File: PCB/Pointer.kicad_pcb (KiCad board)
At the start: 2 copper layers, 81.3 x 63.5 mm, 9 parts, among them J1 Conn_01x20, J2 Conn_01x20, J3 Conn_01x05_Pin, J4 Screw_Terminal_01x02, J5 Conn_01x03_Pin, U1 ULN2003

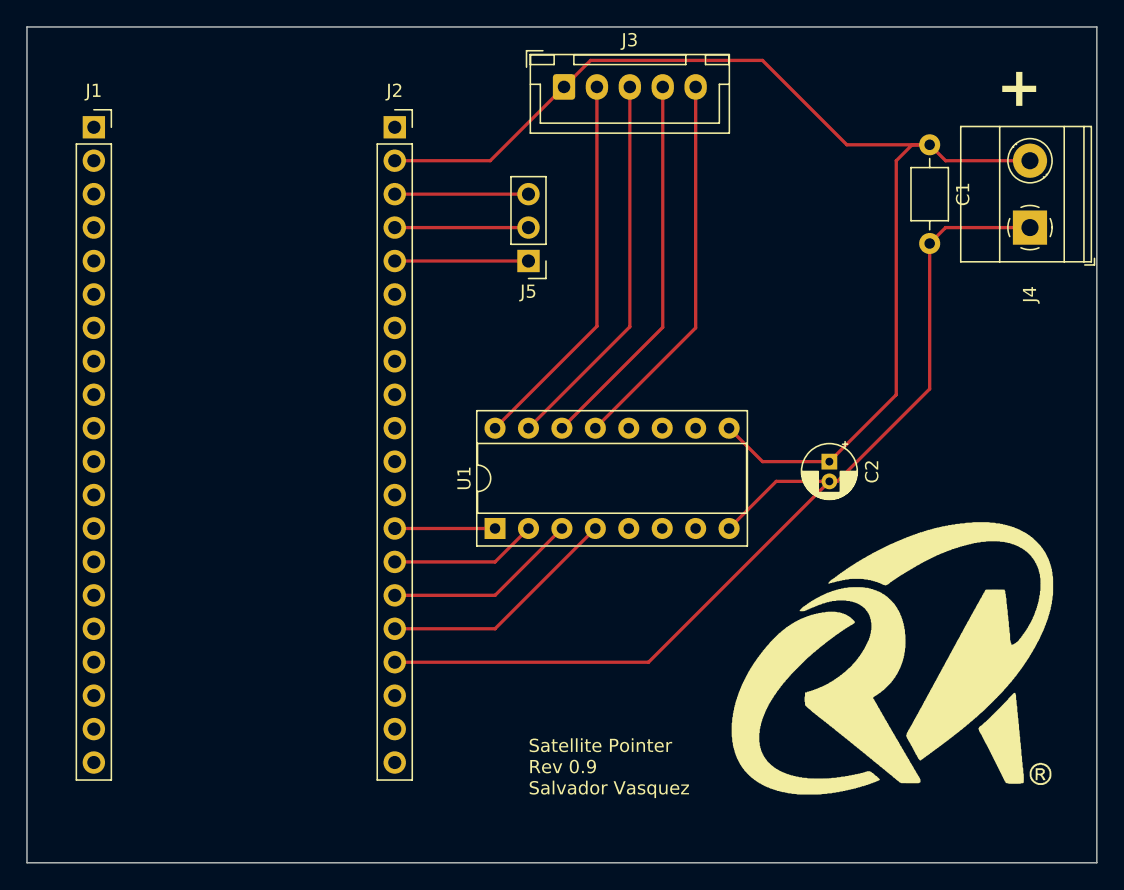
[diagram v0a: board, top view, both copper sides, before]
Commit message: PCB Rev 1.0
Fixed MCU and servo headers
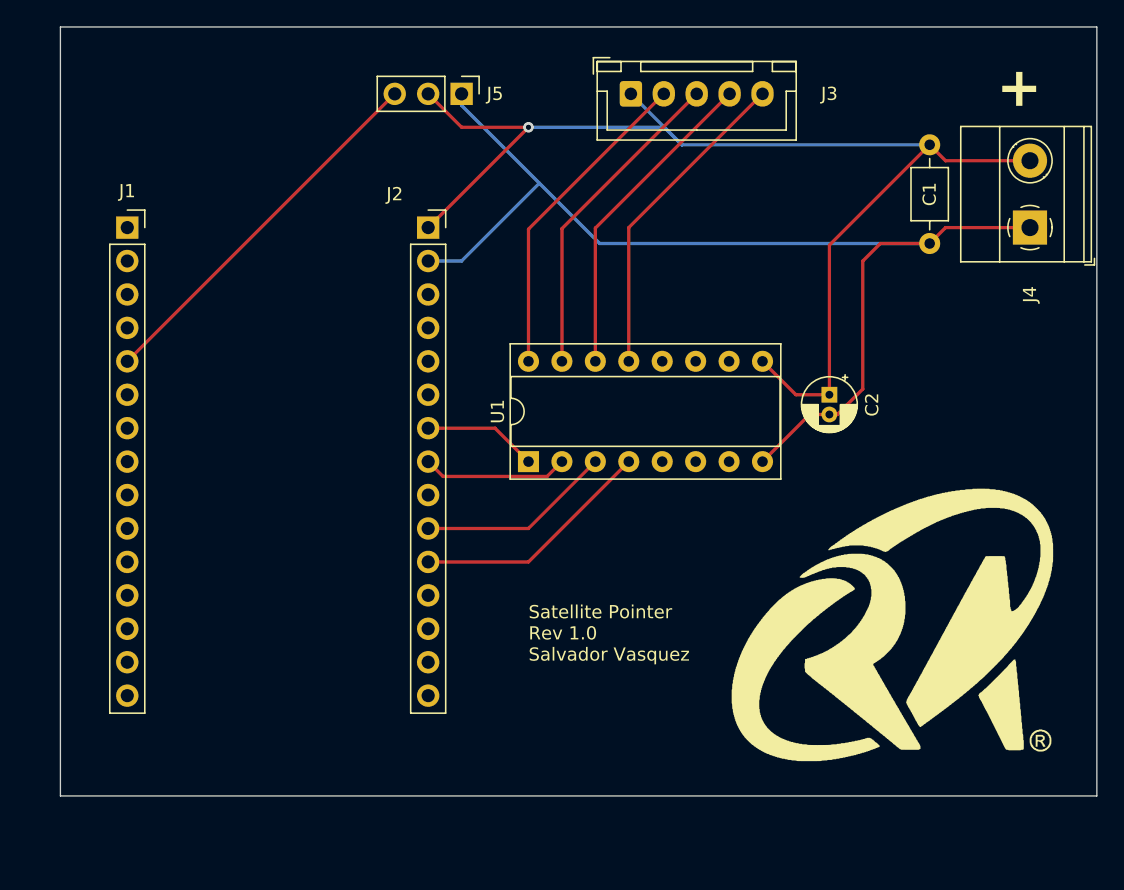
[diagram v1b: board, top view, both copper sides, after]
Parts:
- J1, J2: value Conn_01x20 -> Conn_01x15_Socket; footprint Connector_PinSocket_2.54mm:PinSocket_1x20_P2.54mm_Vertical -> Connector_PinSocket_2.54mm:PinSocket_1x15_P2.54mm_Vertical
- moved J5 13.7 mm to (119.4, 45.7), turned to -90 degrees
- moved J1 8.03 mm to (94.0, 55.9)
- moved J2 8.03 mm to (116.8, 55.9)
- moved U1 5.68 mm to (124.5, 73.7)
- moved J3 5.11 mm to (132.2, 45.7)
- moved C2 5.08 mm to (147.3, 68.6)
- moved Logo 2.54 mm to (152.4, 86.4)
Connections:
- C1 pad 1: Net-(J2-Pin_2) -> Net-(J2-Pin_1)
- C2 pad 1: Net-(J2-Pin_2) -> Net-(J2-Pin_1)
- J1 pad 5: unconnected-(J1-Pin_5-Pad5) -> Net-(J1-Pin_5)
- J2 pad 1: unconnected-(J2-Pin_1-Pad1) -> Net-(J2-Pin_1)
- J2 pad 10: unconnected-(J2-Pin_10-Pad10) -> Net-(J2-Pin_10)
- J2 pad 11: unconnected-(J2-Pin_11-Pad11) -> Net-(J2-Pin_11)
- J2 pad 13: Net-(J2-Pin_13) -> unconnected-(J2-Pin_13-Pad13)
- J2 pad 14: Net-(J2-Pin_14) -> unconnected-(J2-Pin_14-Pad14)
- J2 pad 15: Net-(J2-Pin_15) -> unconnected-(J2-Pin_15-Pad15)
- J2 pad 2: Net-(J2-Pin_2) -> GND
- J2 pad 3: Net-(J2-Pin_3) -> unconnected-(J2-Pin_3-Pad3)
- J2 pad 4: Net-(J2-Pin_4) -> unconnected-(J2-Pin_4-Pad4)
- J2 pad 5: Net-(J2-Pin_5) -> unconnected-(J2-Pin_5-Pad5)
- J2 pad 7: unconnected-(J2-Pin_7-Pad7) -> Net-(J2-Pin_7)
- J2 pad 8: unconnected-(J2-Pin_8-Pad8) -> Net-(J2-Pin_8)
- J3 pad 1: Net-(J2-Pin_2) -> Net-(J2-Pin_1)
- J4 pad 2: Net-(J2-Pin_2) -> Net-(J2-Pin_1)
- J5 pad 1: Net-(J2-Pin_5) -> GND
- J5 pad 2: Net-(J2-Pin_4) -> Net-(J2-Pin_1)
- J5 pad 3: Net-(J2-Pin_3) -> Net-(J1-Pin_5)
- U1 pad 1: Net-(J2-Pin_13) -> Net-(J2-Pin_7)
- U1 pad 2: Net-(J2-Pin_14) -> Net-(J2-Pin_8)
- U1 pad 3: Net-(J2-Pin_15) -> Net-(J2-Pin_10)
- U1 pad 4: Net-(J2-Pin_16) -> Net-(J2-Pin_11)
- U1 pad 9: Net-(J2-Pin_2) -> Net-(J2-Pin_1)
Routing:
- net Net-(J2-Pin_1): track 0.00 -> 92.4 mm, vias 0 -> 1
- net Net-(J2-Pin_2): track 91.3 -> 0.00 mm
- net Net-(J1-Pin_5): track 0.00 -> 28.7 mm
- net Net-(J2-Pin_11): track 0.00 -> 18.4 mm
- net Net-(J2-Pin_16): track 18.4 -> 0.00 mm
- net Net-(J2-Pin_15): track 14.8 -> 0.00 mm
- net Net-(J2-Pin_10): track 0.00 -> 14.8 mm
- net Net-(J2-Pin_14): track 11.2 -> 0.00 mm
- net Net-(J2-Pin_8): track 0.00 -> 11.1 mm
- net Net-(J2-Pin_5): track 10.2 -> 0.00 mm
- net Net-(J2-Pin_4): track 10.2 -> 0.00 mm
- net Net-(J2-Pin_3): track 10.2 -> 0.00 mm
- net Net-(J2-Pin_7): track 0.00 -> 8.67 mm
- net Net-(J2-Pin_13): track 7.62 -> 0.00 mm
- net GND: track 77.5 -> 85.1 mm
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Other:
- board size 81.3 x 63.5 mm -> 78.7 x 58.4 mm
- board text added: "Satellite Pointer Rev 1.0 Salvador Vasquez"
- board text removed: "Satellite Pointer Rev 0.9 Salvador Vasquez"
